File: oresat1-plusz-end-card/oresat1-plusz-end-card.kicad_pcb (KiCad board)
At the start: 4 copper layers, 99.8 x 94.6 mm, 103 parts, among them J1 J-SAMTEC-TFM-120-01-L-D-RA, J2 M55-7101242R, J3 M55-7101242R, J4 M55-7101242R, J5 M55-7101242R, J6 U.FL-R-SMT-1, Q1 DMP2240UDM, Q11 DMP2240UDM-7, Q2 PMV45EN, Q3 PMV45EN, Q4 PMV45EN, Q6 PMV45EN, Q9 DMP2240UDM-7, U11 MIC842LYC5, U12 MIC842LYC5, U2 MAX7310, U201 TS5A21366, U202 TS5A21366, U203 TS5A21366, U204 TS5A21366

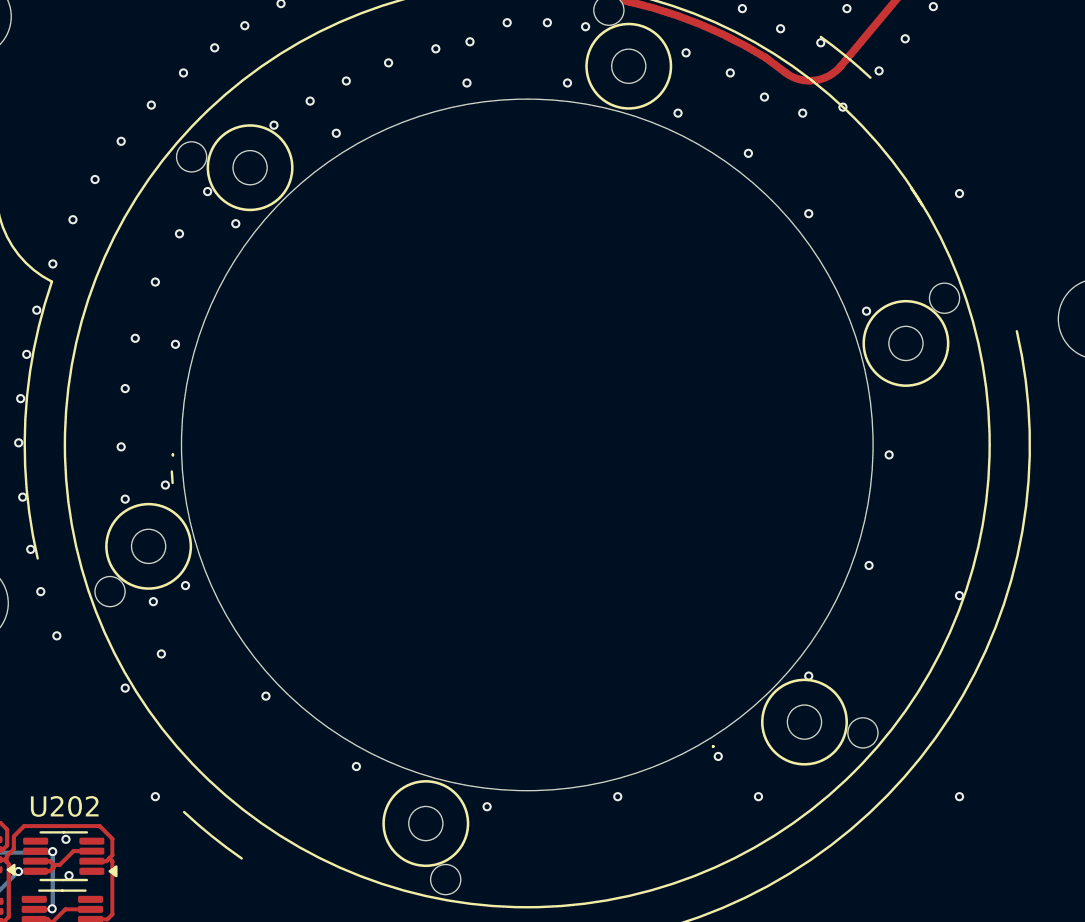
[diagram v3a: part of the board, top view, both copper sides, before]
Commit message: Dipole schematic: added balun & footprints. Pre-tracing
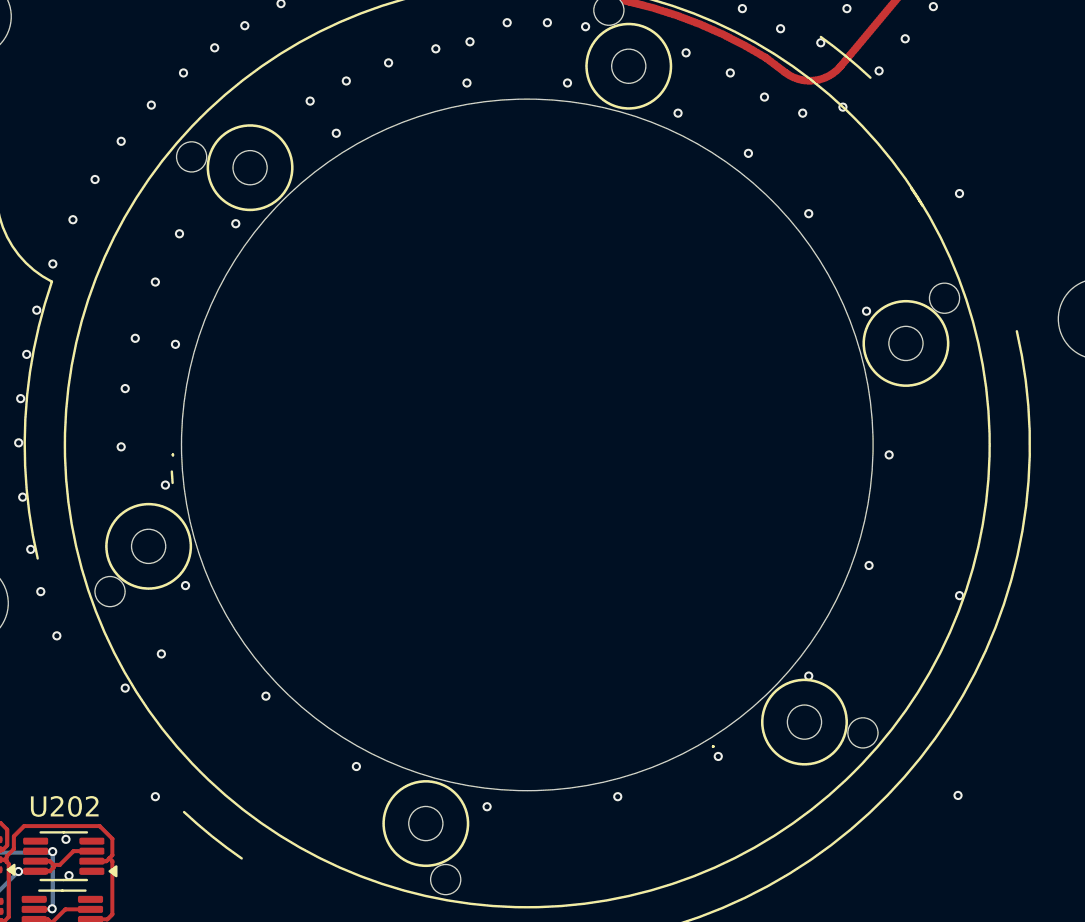
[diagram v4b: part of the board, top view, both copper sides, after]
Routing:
- net GND: vias 280 -> 275
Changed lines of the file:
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@@
 			(solder_mask_margin 0.0635)
 		)
-		(pad "MP" smd rect
+		(pad "SH" smd rect
 			(at -5.67 -2.45 90)
 			(size 1.2 2.7)
 			(layers "F.Cu" "F.Mask" "F.Paste")
+			(net 2 "GND")
+			(pinfunction "MountPin")
+			(pintype "passive")
 			(solder_mask_margin 0.0635)
 		)
-		(pad "MP" smd rect
+		(pad "SH" smd rect
 			(at -5.67 2.45 90)
 			(size 1.2 2.7)
 			(layers "F.Cu" "F.Mask" "F.Paste")
+			(net 2 "GND")
+			(pinfunction "MountPin")
+			(pintype "passive")
 			(solder_mask_margin 0.0635)
 		)
-		(pad "MP" smd rect
+		(pad "SH" smd rect
 			(at 5.67 -2.45 90)
 			(size 1.2 2.7)
 			(layers "F.Cu" "F.Mask" "F.Paste")
+			(net 2 "GND")
+			(pinfunction "MountPin")
+			(pintype "passive")
 			(solder_mask_margin 0.0635)
 		)
-		(pad "MP" smd rect
+		(pad "SH" smd rect
 			(at 5.67 2.45 90)
 			(size 1.2 2.7)
 			(layers "F.Cu" "F.Mask" "F.Paste")
+			(net 2 "GND")
+			(pinfunction "MountPin")
+			(pintype "passive")
 			(solder_mask_margin 0.0635)
 		)
@@
 			)
 		)
-		(property "Datasheet" "~"
+		(property "Datasheet" ""
 			(at 0 0 180)
 			(unlocked yes)
@@
 			)
 		)
-		(property "Datasheet" "~"
+		(property "Datasheet" ""
 			(at 0 0 0)
 			(layer "F.Fab")
@@
 			)
 		)
-		(property "DIS" "DigiKey"
-			(at 0 0 180)
-			(unlocked yes)
-			(layer "F.Fab")
-			(hide yes)
-			(effects
-				(font
-					(size 1 1)
-					(thickness 0.15)
-				)
-			)
-		)
 		(property ki_fp_filters "R_*")
 		(sheetname "/OPD/")
@@
 			)
 		)
-		(property "Datasheet" "~"
+		(property "Datasheet" ""
 			(at 0 0 90)
 			(layer "F.Fab")
@@
 			)
 		)
-		(property "Datasheet" "~"
+		(property "Datasheet" ""
 			(at 0 0 0)
 			(layer "F.Fab")
@@
 			)
 		)
-		(property "DIS" "DigiKey"
-			(at 0 0 0)
-			(unlocked yes)
-			(layer "F.Fab")
-			(hide yes)
-			(effects
-				(font
-					(size 1 1)
-					(thickness 0.15)
-				)
-			)
-		)
 		(property ki_fp_filters "R_*")
 		(sheetname "/OPD/")
@@
 			)
 		)
-		(property "Datasheet" "~"
+		(property "Datasheet" ""
 			(at 0 0 90)
 			(layer "F.Fab")
@@
 			)
 		)
-		(property "Datasheet" "~"
+		(property "Datasheet" ""
 			(at 0 0 0)
 			(layer "F.Fab")
@@
 			)
 		)
-		(property "DIS" "DigiKey"
-			(at 0 0 180)
-			(unlocked yes)
-			(layer "F.Fab")
-			(hide yes)
-			(effects
-				(font
-					(size 1 1)
-					(thickness 0.15)
-				)
-			)
-		)
 		(property ki_fp_filters "R_*")
 		(sheetname "/OPD/")
@@
 			)
 		)
-		(property "Datasheet" "~"
+		(property "Datasheet" ""
 			(at 0 0 0)
 			(unlocked yes)
@@
 			)
 		)
-		(property "Datasheet" "~"
+		(property "Datasheet" ""
 			(at 0 0 0)
 			(unlocked yes)
@@
 			)
 		)
-		(property "Datasheet" "~"
+		(property "Datasheet" ""
 			(at 0 0 0)
 			(layer "F.Fab")
@@
 			)
 		)
-		(property "DIS" "DigiKey"
-			(at 0 0 0)
-			(unlocked yes)
-			(layer "F.Fab")
-			(hide yes)
-			(effects
-				(font
-					(size 1 1)
-					(thickness 0.15)
-				)
-			)
-		)
 		(property ki_fp_filters "R_*")
 		(sheetname "/OPD/")
@@
 			)
 		)
-		(property "Datasheet" "~"
+		(property "Datasheet" ""
 			(at 0 0 90)
 			(layer "F.Fab")
@@
 			)
 		)
-		(property "Datasheet" "~"
+		(property "Datasheet" ""
 			(at 0 0 0)
 			(unlocked yes)
@@
 			)
 		)
-		(property "Datasheet" "~"
+		(property "Datasheet" ""
 			(at 0 0 0)
 			(layer "F.Fab")
@@
 			)
 		)
-		(property "DIS" "DigiKey"
-			(at 0 0 0)
-			(unlocked yes)
-			(layer "F.Fab")
-			(hide yes)
-			(effects
-				(font
-					(size 1 1)
-					(thickness 0.15)
-				)
-			)
-		)
 		(property ki_fp_filters "R_*")
 		(sheetname "/OPD/")
@@
 			)
 		)
-		(property "Datasheet" "~"
+		(property "Datasheet" ""
 			(at 0 0 0)
 			(layer "F.Fab")
@@
 			)
 		)
-		(property "DIS" "DigiKey"
-			(at 0 0 180)
-			(unlocked yes)
-			(layer "F.Fab")
-			(hide yes)
-			(effects
-				(font
-					(size 1 1)
-					(thickness 0.15)
-				)
-			)
-		)
 		(property ki_fp_filters "R_*")
 		(sheetname "/OPD/")
@@
 			)
 		)
-		(property "Datasheet" "~"
+		(property "Datasheet" ""
 			(at 0 0 0)
 			(unlocked yes)
@@
 			)
 		)
-		(property "Datasheet" "~"
+		(property "Datasheet" ""
 			(at 0 0 90)
 			(layer "F.Fab")
@@
 			)
 		)
-		(property "Datasheet" "~"
+		(property "Datasheet" ""
 			(at 0 0 180)
 			(unlocked yes)
@@
 			)
 		)
-		(property "Datasheet" "~"
+		(property "Datasheet" ""
 			(at 0 0 180)
 			(unlocked yes)
@@
 			)
 		)
-		(property "Datasheet" "~"
+		(property "Datasheet" ""
 			(at 0 0 180)
 			(unlocked yes)
@@
 	)
 	(via
-		(at 132.6 89.9)
-		(size 0.4572)
-		(drill 0.254)
-		(layers "F.Cu" "B.Cu")
-		(free yes)
-		(net 2)
-	)
-	(via
 		(at 124.4854 130.4798)
 		(size 0.4572)
@@
 	)
 	(via
+		(at 169.926 119.9388)
+		(size 0.4572)
+		(drill 0.254)
+		(layers "F.Cu" "B.Cu")
+		(free yes)
+		(net 2)
+	)
+	(via
 		(at 141.6 83.5)
 		(size 0.4572)
@@
 	)
 	(via
-		(at 135.9 86.6)
-		(size 0.4572)
-		(drill 0.254)
-		(layers "F.Cu" "B.Cu")
-		(free yes)
-		(net 2)
-	)
-	(via
 		(at 139.55 78.9)
 		(size 0.4572)
@@
 	)
 	(via
-		(at 170 120)
-		(size 0.4572)
-		(drill 0.254)
-		(layers "F.Cu" "B.Cu")
-		(net 2)
-	)
-	(via
 		(at 111.1 58.4)
 		(size 0.4572)
@@
 	)
 	(via
-		(at 129.9 110.3)
-		(size 0.4572)
-		(drill 0.254)
-		(layers "F.Cu" "B.Cu")
-		(free yes)
-		(net 2)
-	)
-	(via
 		(at 180 130)
 		(size 0.4572)
@@
 	)
 	(via
-		(at 128.5 105.2)
-		(size 0.4572)
-		(drill 0.254)
-		(layers "F.Cu" "B.Cu")
-		(free yes)
-		(net 2)
-	)
-	(via
 		(at 183.4 76.4)
 		(size 0.4572)
@@
 	)
 	(via
-		(at 160 120)
-		(size 0.4572)
-		(drill 0.254)
-		(layers "F.Cu" "B.Cu")
-		(net 2)
-	)
-	(via
 		(at 145.5 84.5)
 		(size 0.4572)
@@
 		(layers "F.Cu" "B.Cu" "In2.Cu")
 		(hatch none 0.508)
-		(priority 7)
+		(priority 6)
 		(connect_pads yes
 			(clearance 0.2)
@@
 		(net_name "VBUS")
 		(layer "In2.Cu")
-		(hatch none 0.508)
-		(priority 6)
-		(connect_pads yes
+		(hatch edge 0.5)
+		(priority 5)
+		(connect_pads
 			(clearance 0.2)
 		)
-		(min_thickness 0.127)
+		(min_thickness 0.25)
 		(filled_areas_thickness no)
 		(fill yes
-			(thermal_gap 0.177)
-			(thermal_bridge_width 0.177)
-			(smoothing fillet)
-			(radius 0.2)
+			(thermal_gap 0.5)
+			(thermal_bridge_width 0.5)
 		)
 		(polygon
 			(pts
-				(xy 125.5635 65.8365) (xy 148.6635 65.8365) (xy 148.6635 68.4635) (xy 109.626302 68.4635) (xy 104.6635 73.426302)
-				(xy 104.6635 101.6365) (xy 116.8635 101.6365) (xy 116.8635 104.4635) (xy 104.6635 104.4635) (xy 104.6635 117.673698)
-				(xy 130.326302 143.3365) (xy 147.5365 143.3365) (xy 147.5365 133.9365) (xy 150.6635 133.9365) (xy 150.6635 131.8865)
-				(xy 153.009251 131.8865) (xy 170.8865 114.029474) (xy 170.8865 101.0365) (xy 185.2635 101.0365)
-				(xy 185.2635 122.726303) (xy 160.526303 147.4635) (xy 127.373697 147.4635) (xy 100.5365 120.626303)
-				(xy 100.5365 68.773697) (xy 108.973697 60.3365) (xy 125.5635 60.3365)
+				(xy 185.2635 101.0365) (xy 167.0812 101.0365) (xy 167.2844 103.0478) (xy 167.2336 104.8258) (xy 166.9034 107.061)
+				(xy 166.2176 109.093) (xy 165.1 111.3028) (xy 163.3982 114.1222) (xy 164.2618 114.808) (xy 164.6682 115.4938)
+				(xy 164.7444 116.5606) (xy 164.338 117.7544) (xy 163.6776 118.4148) (xy 162.433 118.8212) (xy 161.1122 118.618)
+				(xy 160.401 118.11) (xy 160.0962 117.6274) (xy 158.9278 118.491) (xy 156.5148 119.6086) (xy 154.1018 120.4722)
+				(xy 151.8666 120.9802) (xy 149.0472 121.3866) (xy 146.1262 121.3104) (xy 145.7706 121.285) (xy 145.7452 121.8184)
+				(xy 145.5674 122.4788) (xy 145.1102 123.0122) (xy 144.6784 123.3678) (xy 144.1196 123.6472) (xy 143.4592 123.7742)
+				(xy 142.7226 123.5964) (xy 142.3162 123.4694) (xy 141.859 123.2154) (xy 141.4018 122.555) (xy 141.0716 121.8184)
+				(xy 141.0462 120.9548) (xy 141.351 120.0404) (xy 139.9286 119.4054) (xy 138.5316 118.5926) (xy 136.7536 117.4242)
+				(xy 134.8232 115.6462) (xy 133.2738 113.9698) (xy 132.1054 111.9632) (xy 131.2164 110.5154) (xy 130.81 109.5502)
+				(xy 130.302 109.7788) (xy 129.159 109.8296) (xy 128.016 109.2708) (xy 127.4064 108.2802) (xy 127.254 107.188)
+				(xy 127.4826 106.4514) (xy 127.8636 105.7402) (xy 128.6256 105.2576) (xy 129.5146 105.0544) (xy 129.413 104.5718)
+				(xy 129.3876 101.0365) (xy 129.8702 97.3836) (xy 130.7592 95.377) (xy 131.826 93.3196) (xy 132.5626 92.0242)
+				(xy 133.4262 90.8812) (xy 132.8928 90.3224) (xy 132.3594 89.1286) (xy 132.3848 87.6554) (xy 133.35 86.5886)
+				(xy 134.9502 86.1568) (xy 135.4836 86.2838) (xy 136.5758 86.868) (xy 136.9314 87.2998) (xy 137.4648 86.9188)
+				(xy 138.9634 85.9028) (xy 140.4112 85.217) (xy 141.8336 84.7344) (xy 143.8402 84.0994) (xy 143.1798 81.6864)
+				(xy 142.24 77.2668) (xy 143.7894 76.3524) (xy 145.7706 76.0476) (xy 147.5232 75.8698) (xy 148.6916 75.8444)
+				(xy 148.6635 70.8635) (xy 148.6635 65.8365) (xy 125.5635 65.8365) (xy 125.5635 60.3365) (xy 108.973697 60.3365)
+				(xy 100.5365 68.773697) (xy 100.5365 120.626303) (xy 127.373697 147.4635) (xy 160.526303 147.4635)
+				(xy 185.2635 122.726303)
 			)
 		)

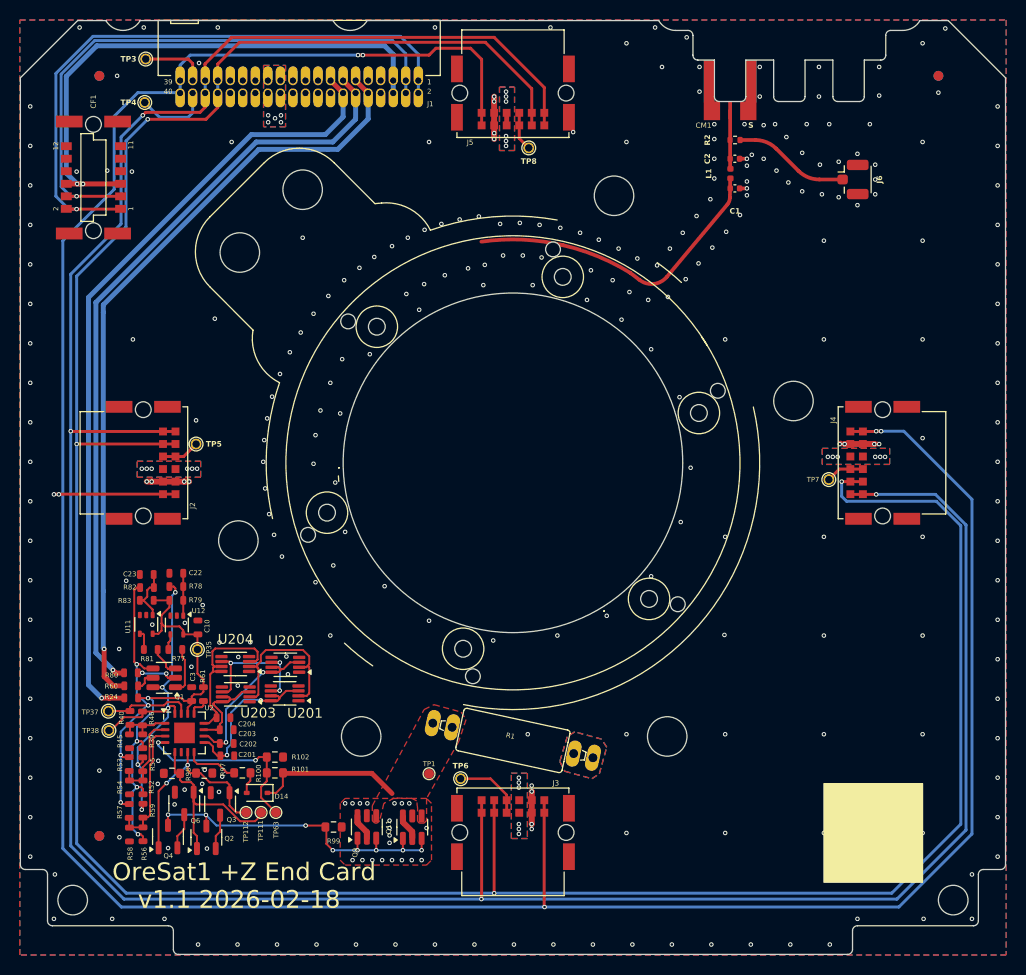
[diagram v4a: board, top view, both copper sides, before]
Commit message: Fixed schematic label issues and routed solar uarts
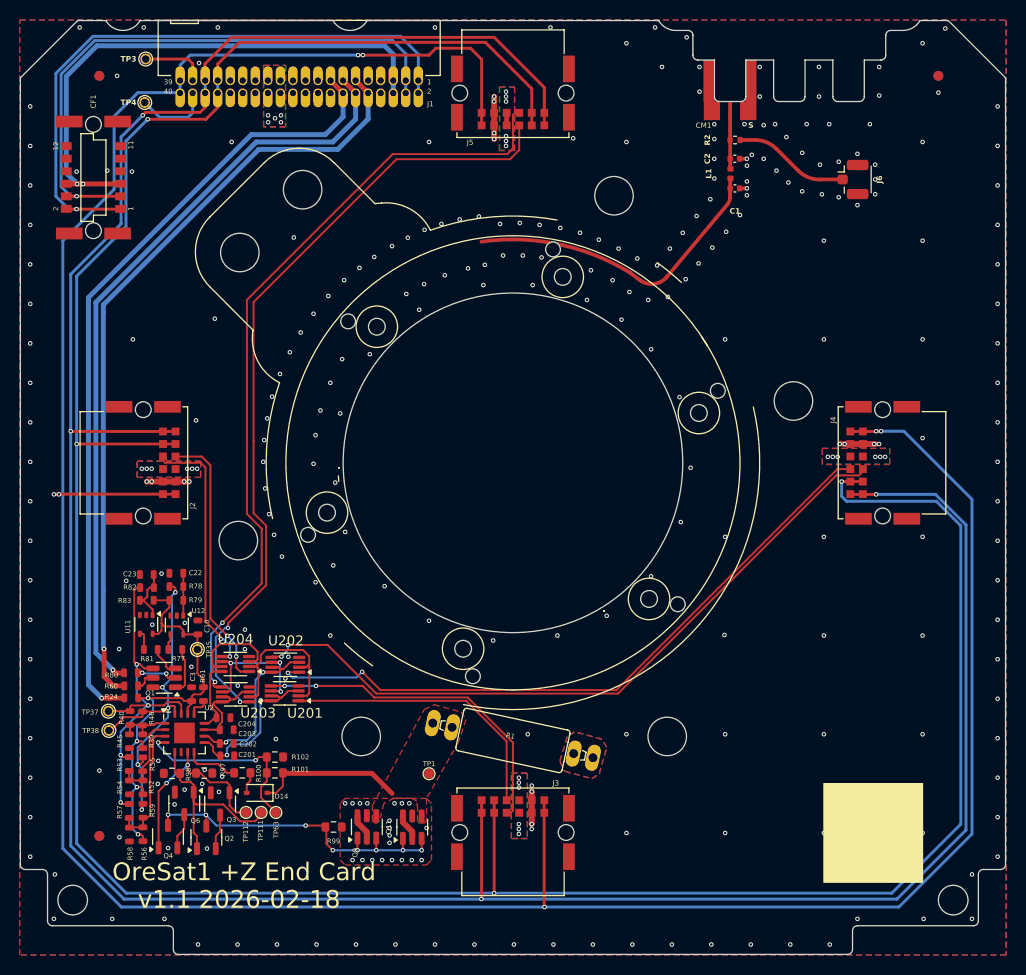
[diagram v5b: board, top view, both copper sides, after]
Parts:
- removed TP5, TP6, TP7, TP8: TestPoint-MinTH, oresat-misc:TestPoint-0.75mm-th
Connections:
- net /OPD/C3-UART-RX renamed /C3_UART_RX
- net /OPD/C3-UART-TX renamed /C3_UART_TX
- net OPD_PWR renamed /OPD_PWR
- net OPD_SCL renamed /OPD_SCL
- net OPD_SDA renamed /OPD_SDA
- J2 pad 7: /-Y_AUX -> /MY-UART-TX
- J2 pad 8: /-Y_AUX -> /MY-UART-RX
- J3 pad 7: /+X_AUX -> /PX_UART_TX
- J3 pad 8: /+X_AUX -> /PX_UART_RX
- J4 pad 7: /+Y_AUX -> /PY_UART_TX
- J4 pad 8: /+Y_AUX -> /PY_UART_RX
- J5 pad 7: /-X_AUX -> /MX_UART_TX
- J5 pad 8: /-X_AUX -> /MX_UART_RX
- U201 pad 1: /OPD/PX-UART-RX -> /PX_UART_RX
- U201 pad 5: /OPD/PX-UART-TX -> /PX_UART_TX
- U202 pad 1: /OPD/PY-UART-RX -> /PY_UART_RX
- U202 pad 5: /OPD/PY-UART-TX -> /PY_UART_TX
- U203 pad 1: /OPD/MX-UART-RX -> /MX_UART_RX
- U203 pad 5: /OPD/MX-UART-TX -> /MX_UART_TX
- U204 pad 1: /OPD/MY-UART-RX -> /MY-UART-RX
- U204 pad 5: /OPD/MY-UART-TX -> /MY-UART-TX
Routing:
- net /MX_UART_RX: track 0.00 -> 81.1 mm, vias 0 -> 2
- net /MX_UART_TX: track 0.00 -> 80.3 mm, vias 0 -> 2
- net /PY_UART_TX: track 0.00 -> 72.3 mm, vias 0 -> 2
- net /PY_UART_RX: track 0.00 -> 68.6 mm, vias 0 -> 2
- net /PX_UART_TX: track 0.00 -> 34.5 mm, vias 0 -> 2
- net /PX_UART_RX: track 0.00 -> 28.8 mm
- net /MY-UART-RX: track 0.00 -> 27.0 mm, vias 0 -> 2
- net /MY-UART-TX: track 0.00 -> 26.2 mm, vias 0 -> 2
- net /+X_AUX: track 7.16 -> 0.00 mm
- net /-Y_AUX: track 4.30 -> 0.00 mm
- net /-X_AUX: track 3.95 -> 0.00 mm
- net /+Y_AUX: track 3.89 -> 0.00 mm
- net /OPD/PY_UART_EN: track 16.4 -> 17.5 mm
- net GND: vias 275 -> 274
